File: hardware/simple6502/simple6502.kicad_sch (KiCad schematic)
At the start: 0 parts

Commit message: Kicad 7 update, 6502 libraries, moved datasheets to their own folder
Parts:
- added U1: W65C02SxP, Package_DIP:DIP-40_W15.24mm, symbol PCM_65xx-library:W65C02SxP
- added U2: CY62256-70PC, Package_DIP:DIP-28_W15.24mm, symbol Memory_RAM:CY62256-70PC
- added U3: 28C256, symbol Memory_EEPROM:28C256
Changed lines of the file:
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@@
-(kicad_sch (version 20211123) (generator eeschema)
+(kicad_sch (version 20230121) (generator eeschema)
   (paper "USLetter")
   (title_block
@@
     (company "Mariano Luna")
   )
+  (symbol (lib_id "Memory_RAM:CY62256-70PC") (at 152.4 63.5 0) (unit 1)
+    (in_bom yes) (on_board yes) (dnp no) (fields_autoplaced)
+    (property "Reference" "U2" (at 154.5941 38.1 0)
+      (effects (font (size 1.27 1.27)) (justify left))
+    )
+    (property "Value" "CY62256-70PC" (at 154.5941 40.64 0)
+      (effects (font (size 1.27 1.27)) (justify left))
+    )
+    (property "Footprint" "Package_DIP:DIP-28_W15.24mm" (at 152.4 66.04 0)
+      (effects (font (size 1.27 1.27)) hide)
+    )
+    (property "Datasheet" "https://ecee.colorado.edu/~mcclurel/Cypress_SRAM_CY62256.pdf" (at 152.4 66.04 0)
+      (effects (font (size 1.27 1.27)) hide)
+    )
+    (pin "14")
+    (pin "28")
+    (pin "1")
+    (pin "10")
+    (pin "11")
+    (pin "12")
+    (pin "13")
+    (pin "15")
+    (pin "16")
+    (pin "17")
+    (pin "18")
+    (pin "19")
+    (pin "2")
+    (pin "20")
+    (pin "21")
+    (pin "22")
+    (pin "23")
+    (pin "24")
+    (pin "25")
+    (pin "26")
+    (pin "27")
+    (pin "3")
+    (pin "4")
+    (pin "5")
+    (pin "6")
+    (pin "7")
+    (pin "8")
+    (pin "9")
+    (instances
+      (project "simple6502"
+        (path "/c0007eb4-077e-4f77-aad9-8dd15548af06"
+          (reference "U2") (unit 1)
+        )
+      )
+    )
+  )
+  (symbol (lib_id "Memory_EEPROM:28C256") (at 210.82 68.58 0) (unit 1)
+    (in_bom yes) (on_board yes) (dnp no) (fields_autoplaced)
+    (property "Reference" "U3" (at 213.0141 38.1 0)
+      (effects (font (size 1.27 1.27)) (justify left))
+    )
+    (property "Value" "28C256" (at 213.0141 40.64 0)
+      (effects (font (size 1.27 1.27)) (justify left))
+    )
+    (property "Footprint" "" (at 210.82 68.58 0)
+      (effects (font (size 1.27 1.27)) hide)
+    )
+    (property "Datasheet" "http://ww1.microchip.com/downloads/en/DeviceDoc/doc0006.pdf" (at 208.28 38.1 0)
+      (effects (font (size 1.27 1.27)) hide)
+    )
+    (pin "1")
+    (pin "10")
+    (pin "11")
+    (pin "12")
+    (pin "13")
+    (pin "14")
+    (pin "15")
+    (pin "16")
+    (pin "17")
+    (pin "18")
+    (pin "19")
+    (pin "2")
+    (pin "20")
+    (pin "21")
+    (pin "22")
+    (pin "23")
+    (pin "24")
+    (pin "25")
+    (pin "26")
+    (pin "27")
+    (pin "28")
+    (pin "3")
+    (pin "4")
+    (pin "5")
+    (pin "6")
+    (pin "7")
+    (pin "8")
+    (pin "9")
+    (instances
+      (project "simple6502"
+        (path "/c0007eb4-077e-4f77-aad9-8dd15548af06"
+          (reference "U3") (unit 1)
+        )
+      )
+    )
+  )
+  (symbol (lib_id "PCM_65xx-library:W65C02SxP") (at 71.12 78.74 0) (unit 1)
+    (in_bom yes) (on_board yes) (dnp no) (fields_autoplaced)
+    (property "Reference" "U1" (at 73.3141 38.1 0)
+      (effects (font (size 1.27 1.27)) (justify left))
+    )
+    (property "Value" "W65C02SxP" (at 73.3141 40.64 0)
+      (effects (font (size 1.27 1.27)) (justify left))
+    )
+    (property "Footprint" "Package_DIP:DIP-40_W15.24mm" (at 71.12 27.94 0)
+      (effects (font (size 1.27 1.27)) hide)
+    )
+    (property "Datasheet" "http://www.westerndesigncenter.com/wdc/documentation/w65c02s.pdf" (at 71.12 30.48 0)
+      (effects (font (size 1.27 1.27)) hide)
+    )
+    (pin "1")
+    (pin "10")
+    (pin "11")
+    (pin "12")
+    (pin "13")
+    (pin "14")
+    (pin "15")
+    (pin "16")
+    (pin "17")
+    (pin "18")
+    (pin "19")
+    (pin "2")
+    (pin "20")
+    (pin "21")
+    (pin "22")
+    (pin "23")
+    (pin "24")
+    (pin "25")
+    (pin "26")
+    (pin "27")
+    (pin "28")
+    (pin "29")
+    (pin "3")
+    (pin "30")
+    (pin "31")
+    (pin "32")
+    (pin "33")
+    (pin "34")
+    (pin "35")
+    (pin "36")
+    (pin "37")
+    (pin "38")
+    (pin "39")
+    (pin "4")
+    (pin "40")
+    (pin "5")
+    (pin "6")
+    (pin "7")
+    (pin "8")
+    (pin "9")
+    (instances
+      (project "simple6502"
+        (path "/c0007eb4-077e-4f77-aad9-8dd15548af06"
+          (reference "U1") (unit 1)
+        )
+      )
+    )
+  )
   (sheet_instances

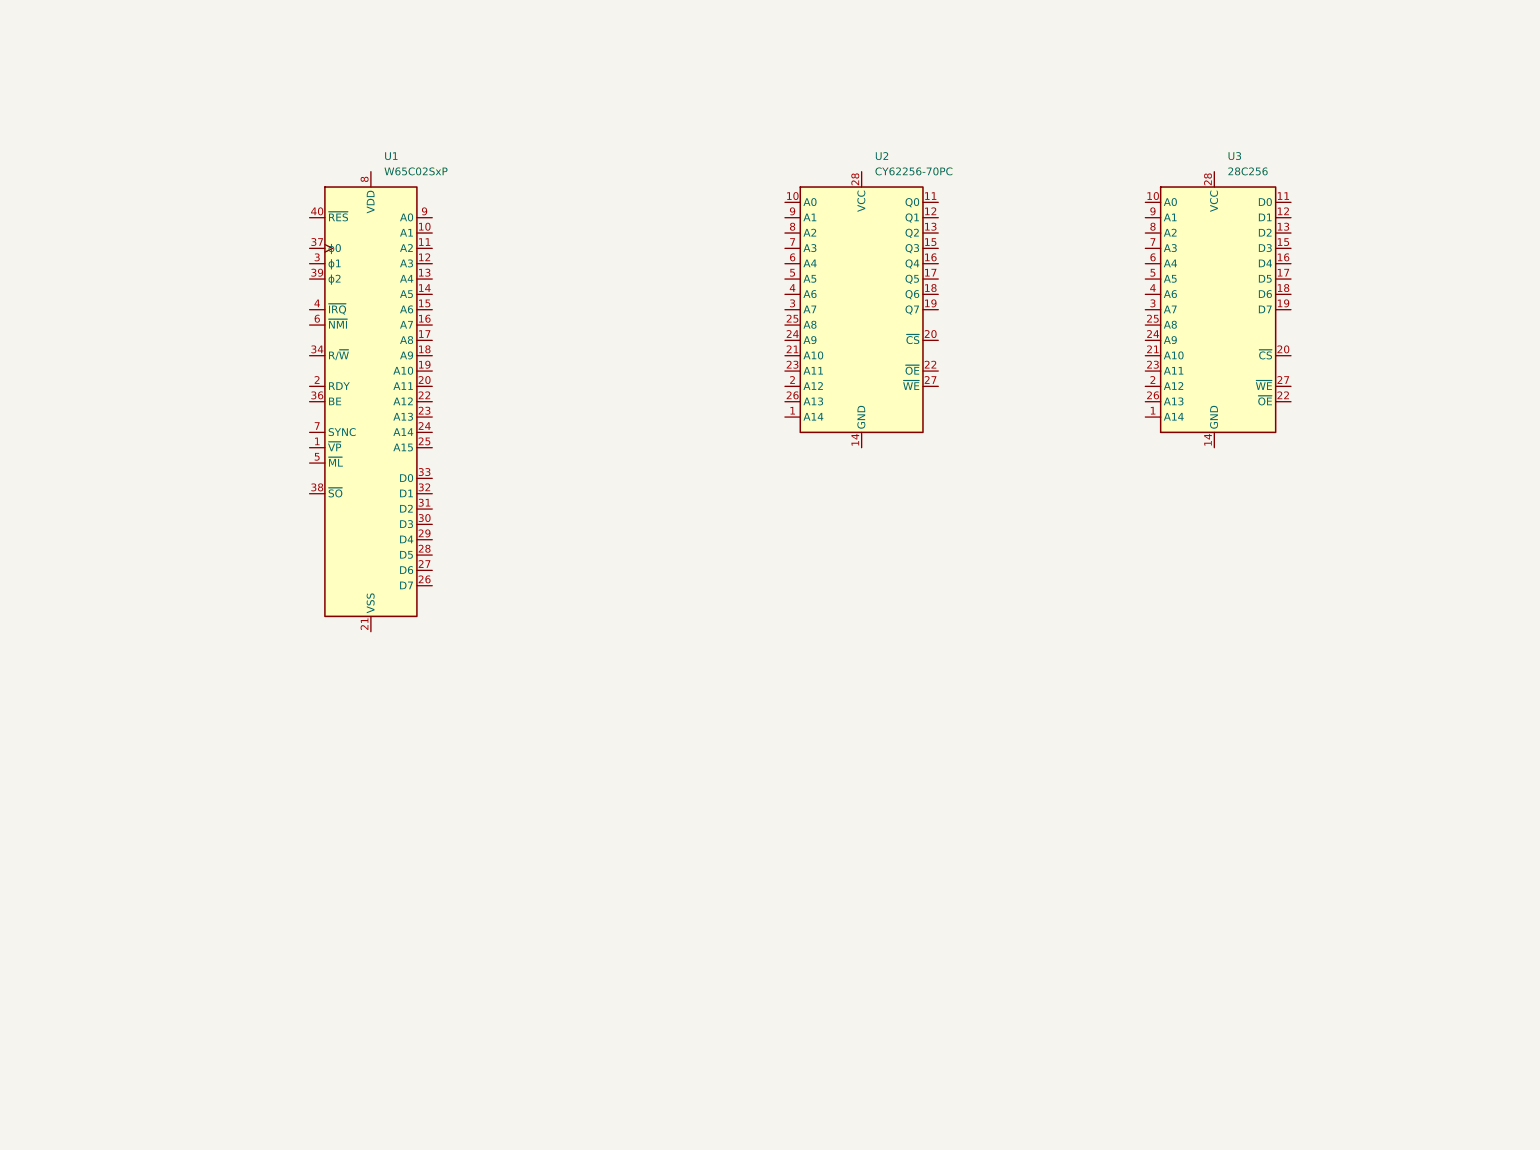
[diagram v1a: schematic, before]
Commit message: Wired CPU, RAM and ROM
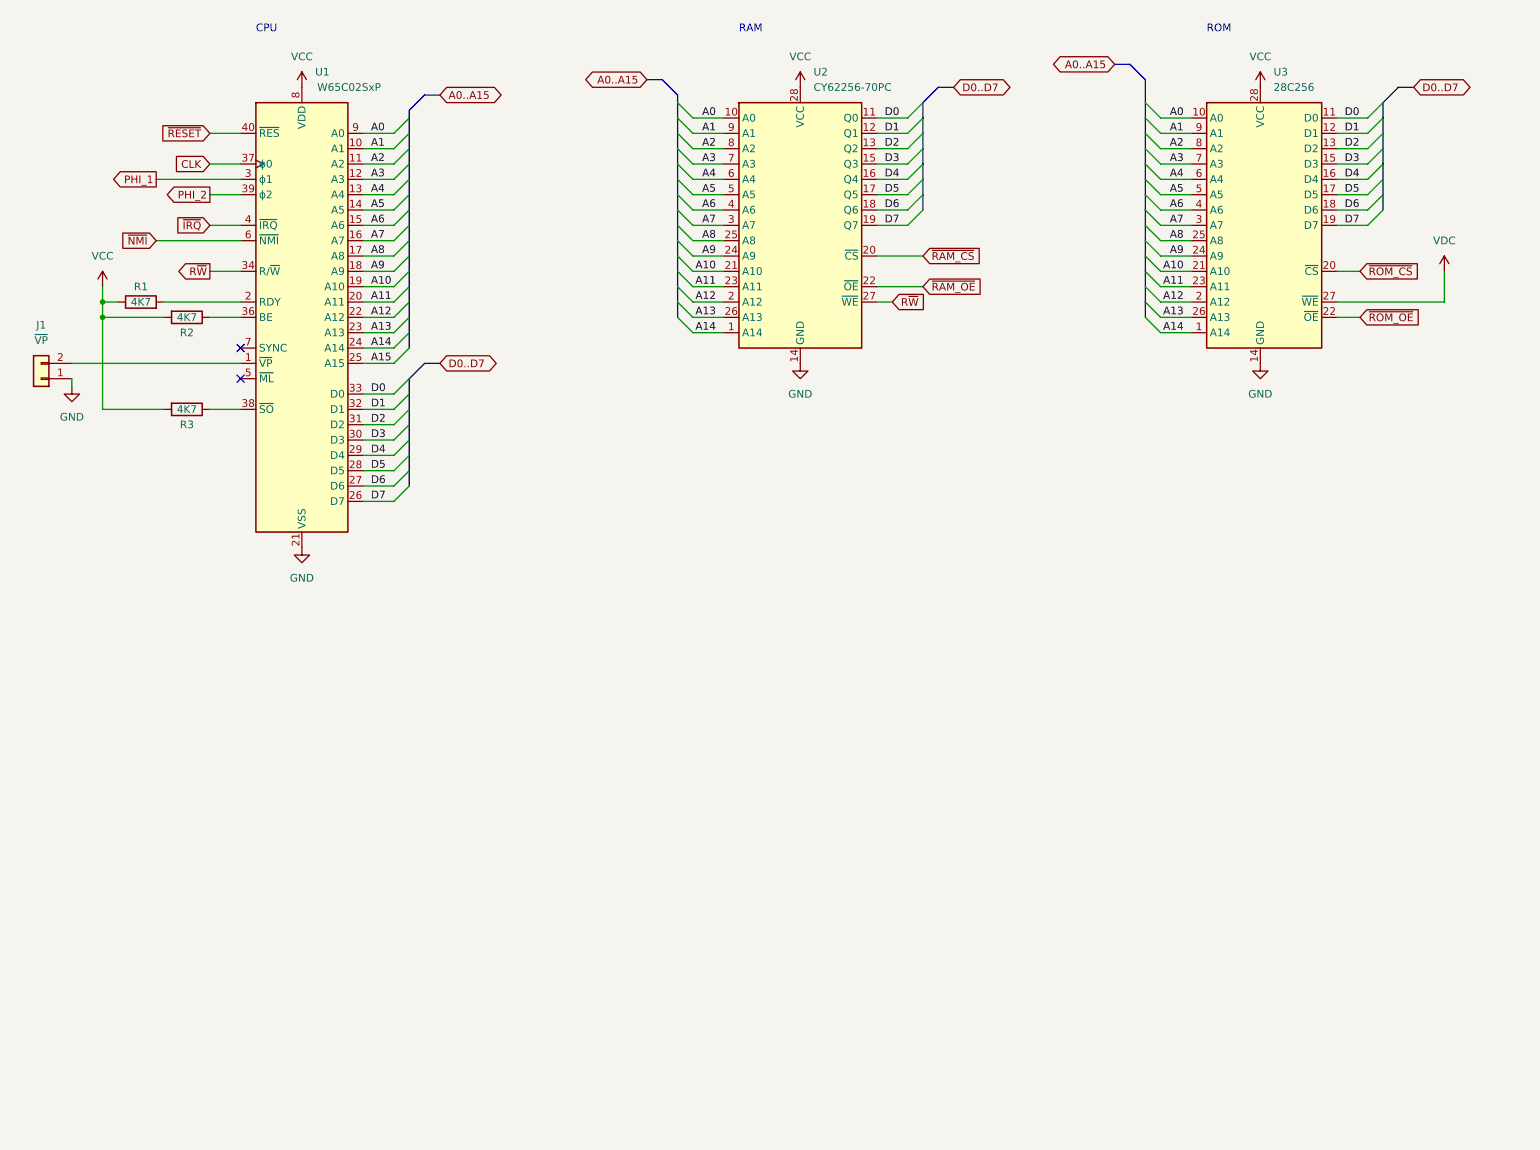
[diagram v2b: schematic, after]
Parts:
- added J1: ~{VP}, symbol Connector_Generic:Conn_01x02
- added R1, R2, R3: 4K7, symbol Device:R
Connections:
- net A14: now reaches U2.1 (A14)
- net A14: now also U1.24 (A14), U3.1 (A14)
- net A0: now reaches U2.10 (A0)
- net A0: now also U1.9 (A0), U3.10 (A0)
- net D0: now reaches U2.11 (Q0)
- net D0: now also U1.33 (D0), U3.11 (D0)
- net D1: now reaches U2.12 (Q1)
- net D1: now also U1.32 (D1), U3.12 (D1)
- net D2: now reaches U2.13 (Q2)
- net D2: now also U1.31 (D2), U3.13 (D2)
- net GND: now reaches U2.14 (GND)
- net GND: now also U1.21 (VSS), U3.14 (GND), J1.1 (Pin_1)
- net D3: now reaches U2.15 (Q3)
- net D3: now also U1.30 (D3), U3.15 (D3)
- net D4: now reaches U2.16 (Q4)
- net D4: now also U1.29 (D4), U3.16 (D4)
- net D5: now reaches U2.17 (Q5)
- net D5: now also U1.28 (D5), U3.17 (D5)
- net D6: now reaches U2.18 (Q6)
- net D6: now also U1.27 (D6), U3.18 (D6)
- net D7: now reaches U2.19 (Q7)
- net D7: now also U1.26 (D7), U3.19 (D7)
- net A12: now reaches U2.2 (A12)
- net A12: now also U1.22 (A12), U3.2 (A12)
- net ~{RAM_CS}: now reaches U2.20 (~{CS})
- net A10: now reaches U2.21 (A10)
- net A10: now also U1.19 (A10), U3.21 (A10)
- net ~{RAM_OE}: now reaches U2.22 (~{OE})
- net A11: now reaches U2.23 (A11)
- net A11: now also U1.20 (A11), U3.23 (A11)
- net A9: now reaches U2.24 (A9)
- net A9: now also U1.18 (A9), U3.24 (A9)
- net A8: now reaches U2.25 (A8)
- net A8: now also U1.17 (A8), U3.25 (A8)
- net A13: now reaches U2.26 (A13)
- net A13: now also U1.23 (A13), U3.26 (A13)
- net R~{W}: now reaches U2.27 (~{WE})
- net R~{W}: now also U1.34 (R/~{W})
- net VCC: now reaches U2.28 (VCC)
- net VCC: now also U1.8 (VDD), U3.28 (VCC), R1.1, R2.2, R3.2
- net A7: now reaches U2.3 (A7)
- net A7: now also U1.16 (A7), U3.3 (A7)
- net A6: now reaches U2.4 (A6)
- net A6: now also U1.15 (A6), U3.4 (A6)
- net A5: now reaches U2.5 (A5)
- net A5: now also U1.14 (A5), U3.5 (A5)
- net A4: now reaches U2.6 (A4)
- net A4: now also U1.13 (A4), U3.6 (A4)
- net A3: now reaches U2.7 (A3)
- net A3: now also U1.12 (A3), U3.7 (A3)
- net A2: now reaches U2.8 (A2)
- net A2: now also U1.11 (A2), U3.8 (A2)
- net A1: now reaches U2.9 (A1)
- net A1: now also U1.10 (A1), U3.9 (A1)
- net ~{ROM_CS}: now reaches U3.20 (~{CS})
- net ~{ROM_OE}: now reaches U3.22 (~{OE})
- net VDC: now reaches U3.27 (~{WE})
- net at U1.1 (~{VP}): now also J1.2 (Pin_2)
- net at U1.2 (RDY): now also R1.2
- net A15: now reaches U1.25 (A15)
- net PHI_1: now reaches U1.3 (ϕ1)
- net at U1.36 (BE): now also R2.1
- net CLK: now reaches U1.37 (ϕ0)
- net at U1.38 (~{SO}): now also R3.1
- net PHI_2: now reaches U1.39 (ϕ2)
- net ~{IRQ}: now reaches U1.4 (~{IRQ})
- net ~{RESET}: now reaches U1.40 (~{RES})
- net ~{NMI}: now reaches U1.6 (~{NMI})
- no-connect marks 0 -> 2
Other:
- note added: "CPU"
- note added: "RAM"
- note added: "ROM"
- moved on the sheet: U1, U2, U3

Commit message: Reset, Clock, Expansion and Power
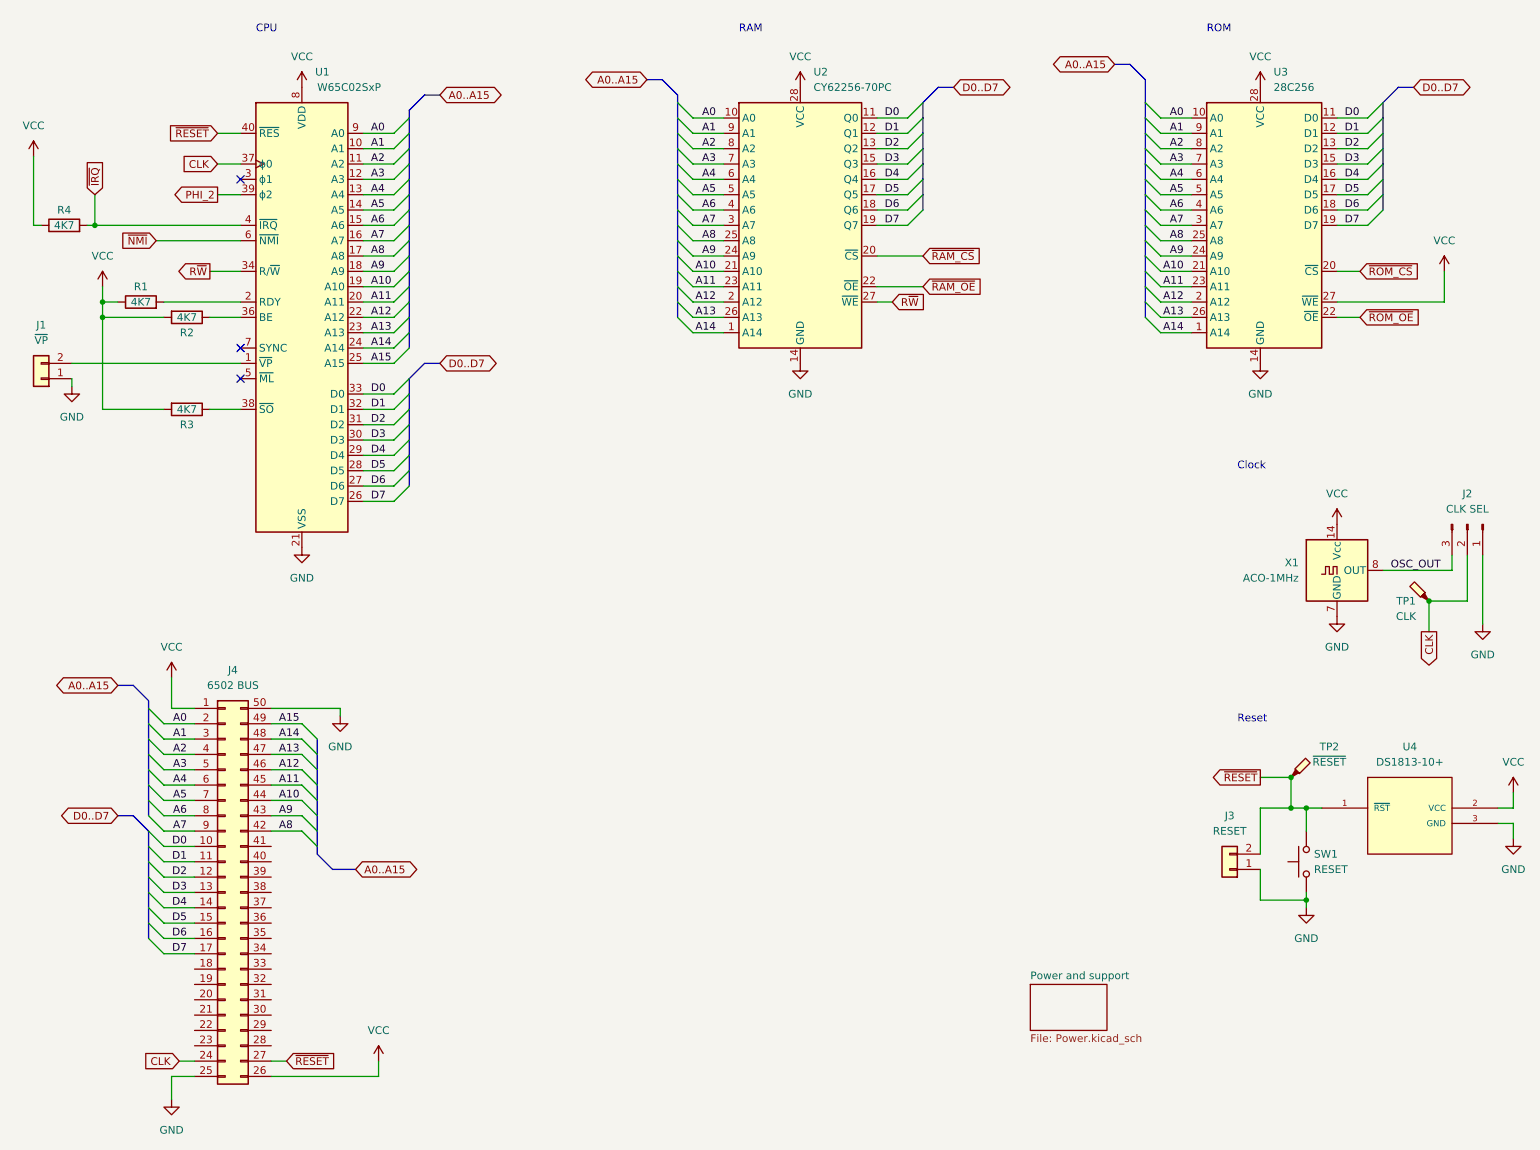
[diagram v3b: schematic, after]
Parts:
- added J2: CLK SEL, symbol Connector:Conn_01x03_Pin
- added J3: RESET, symbol Connector_Generic:Conn_01x02
- added J4: 6502 BUS, symbol Connector_Generic:Conn_02x25_Counter_Clockwise
- added R4: 4K7, symbol Device:R
- added SW1: RESET, symbol Switch:SW_Push
- added TP1: CLK, symbol Connector:TestPoint_Probe
- added TP2: ~{RESET}, symbol Connector:TestPoint_Probe
- added U4: DS1813-10+, DS1813-10+:21-0248A, symbol DS1813-10_:DS1813-10+
- added X1: ACO-1MHz, Oscillator:Oscillator_DIP-14, symbol Oscillator:ACO-xxxMHz
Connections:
- net VDC is gone; now on net VCC: U3.27 (~{WE})
- net A0: now also J4.2 (Pin_2)
- net A1: now also J4.3 (Pin_3)
- net A10: now also J4.44 (Pin_44)
- net A11: now also J4.45 (Pin_45)
- net A12: now also J4.46 (Pin_46)
- net A13: now also J4.47 (Pin_47)
- net A14: now also J4.48 (Pin_48)
- net A15: now also J4.49 (Pin_49)
- net A2: now also J4.4 (Pin_4)
- net A3: now also J4.5 (Pin_5)
- net A4: now also J4.6 (Pin_6)
- net A5: now also J4.7 (Pin_7)
- net A6: now also J4.8 (Pin_8)
- net A7: now also J4.9 (Pin_9)
- net A8: now also J4.42 (Pin_42)
- net A9: now also J4.43 (Pin_43)
- net CLK: now also J2.2 (Pin_2), J4.24 (Pin_24), TP1.1
- net D0: now also J4.10 (Pin_10)
- net D1: now also J4.11 (Pin_11)
- net D2: now also J4.12 (Pin_12)
- net D3: now also J4.13 (Pin_13)
- net D4: now also J4.14 (Pin_14)
- net D5: now also J4.15 (Pin_15)
- net D6: now also J4.16 (Pin_16)
- net D7: now also J4.17 (Pin_17)
- net GND: now also J2.1 (Pin_1), J3.1 (Pin_1), J4.25 (Pin_25), J4.50 (Pin_50), SW1.1, U4.3 (GND), X1.7 (GND)
- net VCC: now also J4.1 (Pin_1), J4.26 (Pin_26), R4.1, U4.2 (VCC), X1.14 (Vcc)
- net ~{IRQ}: now also R4.2
- net ~{RESET}: now also J3.2 (Pin_2), J4.27 (Pin_27), SW1.2, TP2.1, U4.1 (~{RST})
- net PHI_1: no longer names the net of U1.3 (ϕ1)
- new net OSC_OUT: J2.3 (Pin_3), X1.8 (OUT)
- no-connect marks 2 -> 3
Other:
- added sheet Power and support (Power.kicad_sch)
- note added: "Clock"
- note added: "Reset"
